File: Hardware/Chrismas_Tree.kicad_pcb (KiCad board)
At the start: 2 copper layers, 191 parts, among them U1 PIC18F23K22

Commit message: Added light bulbs schematic.
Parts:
- moved R75 7.62 mm to (176.5, 330.2), turned to 270 degrees
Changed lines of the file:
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@@
   )
   (module Resistor_THT:R_Axial_DIN0207_L6.3mm_D2.5mm_P7.62mm_Horizontal (layer B.Cu)
-    (at 176.53 337.82 90)
+    (at 176.53 330.2 270)
     (descr "Resistor, Axial_DIN0207 series, Axial, Horizontal, pin pitch=7.62mm, 0.25W = 1/4W, length*diameter=6.3*2.5mm^2, http://cdn-reichelt.de/documents/datenblatt/B400/1_4W%23YAG.pdf")
     (tags "Resistor Axial_DIN0207 series Axial Horizontal pin pitch 7.62mm 0.25W = 1/4W length 6.3mm diameter 2.5mm")
@@
     (fp_line (start 0.66 -1.25) (end 6.96 -1.25) (layer B.Fab) (width 0.1))
     (fp_line (start 0.66 1.25) (end 0.66 -1.25) (layer B.Fab) (width 0.1))
-    (pad 2 thru_hole oval (at 7.62 0 90) (size 1.6 1.6) (drill 0.8) (layers *.Cu *.Mask)
+    (pad 2 thru_hole oval (at 7.62 0 270) (size 1.6 1.6) (drill 0.8) (layers *.Cu *.Mask)
       (net 76 "Net-(D75-Pad2)"))
-    (pad 1 thru_hole circle (at 0 0 90) (size 1.6 1.6) (drill 0.8) (layers *.Cu *.Mask)
+    (pad 1 thru_hole circle (at 0 0 270) (size 1.6 1.6) (drill 0.8) (layers *.Cu *.Mask)
       (net 83 +5V))
     (model ${KISYS3DMOD}/Resistor_THT.3dshapes/R_Axial_DIN0207_L6.3mm_D2.5mm_P7.62mm_Horizontal.wrl

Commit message: Reorganized light bulbs connections to ease routing and placed microcontroller and related parts.
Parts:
- added C1: 100n-25V, Capacitor_THT:C_Disc_D5.0mm_W2.5mm_P5.00mm, B.Cu at (172.7, 210.8)
- added C2: 1u-25V, Capacitor_THT:C_Disc_D5.0mm_W2.5mm_P5.00mm, B.Cu at (172.7, 215.9)
- added C3: 10u-25V, Capacitor_THT:C_Disc_D5.0mm_W2.5mm_P5.00mm, B.Cu at (180.3, 213.4)
- added C4: 100n-25V, Capacitor_THT:C_Disc_D5.0mm_W2.5mm_P5.00mm, B.Cu at (157.5, 259.1)
- added J1: DNP, Connector_PinHeader_2.54mm:PinHeader_1x05_P2.54mm_Vertical, F.Cu at (167.6, 251.5)
- added Q1: BC548, Package_TO_SOT_THT:TO-92_Inline, B.Cu at (152.4, 17.8)
- added R96: 180, Resistor_THT:R_Axial_DIN0207_L6.3mm_D2.5mm_P7.62mm_Horizontal, B.Cu at (157.5, 182.9)
- added R97: 220, Resistor_THT:R_Axial_DIN0207_L6.3mm_D2.5mm_P7.62mm_Horizontal, B.Cu at (152.4, 241.3)
- added R98: 10K, Resistor_THT:R_Axial_DIN0207_L6.3mm_D2.5mm_P7.62mm_Horizontal, B.Cu at (160.0, 246.4)
- D92, D93, D94, D95: value LED -> RED
- R82, R83, R84, R85, R86, R87, R88, R89, R90, R91, R92, R93, R94, R95: value R -> 220; moved to B.Cu
- U1: moved to B.Cu
- moved R92 339.9 mm to (142.2, 10.2)
- moved R93 321.2 mm to (180.3, 10.2), turned to 180 degrees
- moved U1 309.2 mm to (157.5, 231.1)
- moved R94 297.7 mm to (175.3, 17.8), turned to 180 degrees
- moved R90 236.2 mm to (142.2, 215.9), turned to 180 degrees
- moved R95 224.9 mm to (175.3, 2.54), turned to 180 degrees
- moved R86 219.7 mm to (142.2, 205.7), turned to 180 degrees
- moved R88 219.4 mm to (142.2, 210.8), turned to 180 degrees
- moved R84 214.4 mm to (147.3, 203.2), turned to 90 degrees
- moved R83 209.1 mm to (165.1, 190.5), turned to 90 degrees
- moved R82 209.1 mm to (152.4, 200.7), turned to 90 degrees
- moved R85 202.4 mm to (170.2, 200.7), turned to 90 degrees
- moved R87 201.1 mm to (180.3, 203.2)
- moved R89 187.1 mm to (180.3, 226.1)
- moved R91 186.4 mm to (180.3, 233.7)
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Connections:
- D92 pad 1: GND -> Net-(D92-Pad1)
- D93 pad 1: GND -> Net-(D92-Pad1)
- D94 pad 1: GND -> Net-(D92-Pad1)
- D95 pad 1: GND -> Net-(D92-Pad1)
- R82 pad 1: Net-(R82-Pad1) -> /Light bulbs/Bulb_0
- R83 pad 1: Net-(R82-Pad1) -> /Light bulbs/Bulb_9
- R84 pad 1: Net-(R82-Pad1) -> /Light bulbs/Bulb_1
- R85 pad 1: Net-(R82-Pad1) -> /Light bulbs/Bulb_8
- R86 pad 1: Net-(R82-Pad1) -> /Light bulbs/Bulb_2
- R87 pad 1: Net-(R82-Pad1) -> /Light bulbs/Bulb_7
- R88 pad 1: Net-(R82-Pad1) -> /Light bulbs/Bulb_3
- R89 pad 1: Net-(R82-Pad1) -> /Light bulbs/Bulb_6
- R90 pad 1: Net-(R82-Pad1) -> /Light bulbs/Bulb_4
- R91 pad 1: Net-(R82-Pad1) -> /Light bulbs/Bulb_5
- R92 pad 1: Net-(R82-Pad1) -> +5V
- R93 pad 1: Net-(R82-Pad1) -> +5V
- R94 pad 1: Net-(R82-Pad1) -> +5V
- R95 pad 1: Net-(R82-Pad1) -> +5V
- U1 pad 10: Net-(U1-Pad10) -> /Light bulbs/Bulb_3
- U1 pad 11: Net-(U1-Pad11) -> /Light bulbs/Bulb_2
- U1 pad 12: Net-(U1-Pad12) -> /Light bulbs/Bulb_1
- U1 pad 13: Net-(U1-Pad13) -> /Light bulbs/Bulb_0
- U1 pad 14: Net-(U1-Pad14) -> /Light bulbs/Star
- U1 pad 15: Net-(U1-Pad15) -> /Light bulbs/Bulb_9
- U1 pad 16: Net-(U1-Pad16) -> /Light bulbs/Bulb_8
- U1 pad 17: Net-(U1-Pad17) -> /Light bulbs/Bulb_7
- U1 pad 19: Net-(U1-Pad19) -> GND
- U1 pad 20: Net-(U1-Pad20) -> +5V
- U1 pad 25: Net-(U1-Pad25) -> /Light bulbs/Bulb_6
- U1 pad 26: Net-(U1-Pad26) -> /Light bulbs/Bulb_5
- U1 pad 8: Net-(U1-Pad8) -> GND
- U1 pad 9: Net-(U1-Pad9) -> /Light bulbs/Bulb_4
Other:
- board text added: "/MCLR"

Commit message: Set foliage and trunk leds color.
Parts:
- D1, D10, D11, D12, D14, D15, D16, D18, D19, D2, D20, D22, D23, D24, D26, D27, D28, D3, D30, D31, D32, D34, D35, D36, D38, D39, D40, D42, D43, D44, D46, D47, D48, D50, D51, D52, D53, D54, D55, D56, D57, D58, D59, D6, D60, D61, D62, D63, D64, D65, D66, D67, D68, D69, D7, D70, D71, D72, D73, D74, D75, D76, D77, D78, D79, D8, D80, D81: value LED -> Green
- D13, D17, D21, D25, D29, D33, D37, D4, D41, D45, D49, D5, D9: value LED -> Amber
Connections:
- R13 pad 1: +5V -> Net-(R13-Pad1)
- R17 pad 1: +5V -> Net-(R13-Pad1)
- R21 pad 1: +5V -> Net-(R13-Pad1)
- R25 pad 1: +5V -> Net-(R13-Pad1)
- R29 pad 1: +5V -> Net-(R13-Pad1)
- R33 pad 1: +5V -> Net-(R13-Pad1)
- R37 pad 1: +5V -> Net-(R13-Pad1)
- R4 pad 1: +5V -> Net-(R13-Pad1)
- R41 pad 1: +5V -> Net-(R13-Pad1)
- R45 pad 1: +5V -> Net-(R13-Pad1)
- R49 pad 1: +5V -> Net-(R13-Pad1)
- R5 pad 1: +5V -> Net-(R13-Pad1)
- R9 pad 1: +5V -> Net-(R13-Pad1)

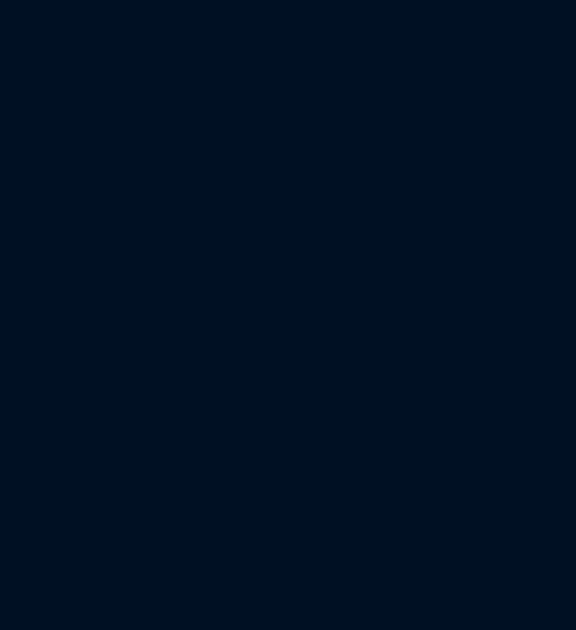
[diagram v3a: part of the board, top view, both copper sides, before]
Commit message: Added micro USB B connector for power supply.
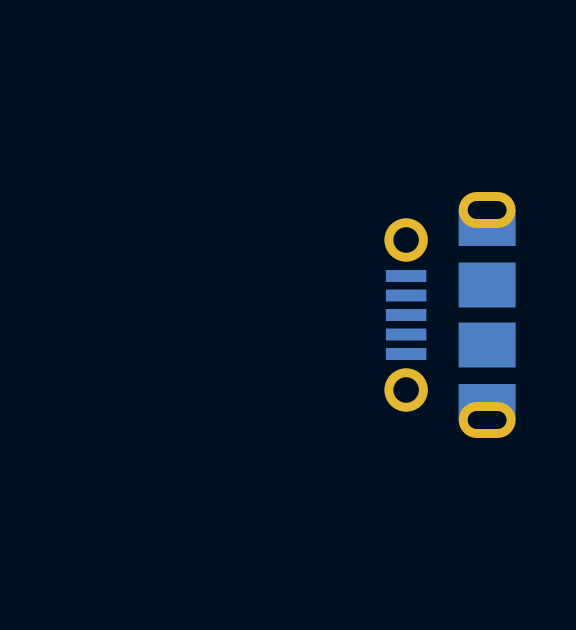
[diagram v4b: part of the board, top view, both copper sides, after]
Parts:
- added J2: USB_B_Micro, Connector_USB:USB_Micro-B_Molex-105017-0001, B.Cu at (289.6, 330.2)
- R1, R10, R11, R12, R13, R14, R15, R16, R17, R18, R19, R2, R20, R21, R22, R23, R24, R25, R26, R27, R28, R29, R3, R30, R31, R32, R33, R34, R35, R36, R37, R38, R39, R4, R40, R41, R42, R43, R44, R45, R46, R47, R48, R49, R5, R50, R51, R52, R53, R54, R55, R56, R57, R58, R59, R6, R60, R61, R62, R63, R64, R65, R66, R67, R68, R69, R7, R70, R71, R72, R73, R74, R75, R76, R77, R78, R79, R8, R80, R81, R9: value R -> 180

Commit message: Routed whole circuit and added ground planes.
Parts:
- moved J2 3.81 mm to (285.8, 330.2)
- renumbered D38 to D10, D42 to D11, D46 to D12, D50 to D13, D53 to D14, D56 to D15, D59 to D16, D62 to D17, D65 to D18, D68 to D19, D6 to D2, D71 to D20, D74 to D21, D76 to D22, D78 to D23, D80 to D24, D2 to D25, D7 to D26, D11 to D27, D15 to D28, D19 to D29, D10 to D3, D23 to D30, D27 to D31, D31 to D32, D35 to D33, D39 to D34, D43 to D35, D47 to D36, D51 to D37, D54 to D38, D57 to D39, D14 to D4, D60 to D40, D63 to D41, D66 to D42, D69 to D43, D72 to D44, D75 to D45, D77 to D46, D79 to D47, D81 to D48, D3 to D49, D18 to D5, D8 to D50, D12 to D51, D16 to D52, D20 to D53, D24 to D54, D28 to D55, D32 to D56, D36 to D57, D40 to D58, D44 to D59, D22 to D6, D48 to D60, D52 to D61, D55 to D62, D58 to D63, D61 to D64, D64 to D65, D67 to D66, D70 to D67, D73 to D68, D4 to D69, D26 to D7, D5 to D70, D9 to D71, D13 to D72, D17 to D73, D21 to D74, D25 to D75, D29 to D76, D33 to D77, D37 to D78, D41 to D79, D30 to D8, D45 to D80, D49 to D81, D34 to D9, R38 to R10, R42 to R11, R46 to R12, R50 to R13, R53 to R14, R56 to R15, R59 to R16, R62 to R17, R65 to R18, R68 to R19, R6 to R2, R71 to R20, R74 to R21, R76 to R22, R78 to R23, R80 to R24, R2 to R25, R7 to R26, R11 to R27, R15 to R28, R19 to R29, R10 to R3, R23 to R30, R27 to R31, R31 to R32, R35 to R33, R39 to R34, R43 to R35, R47 to R36, R51 to R37, R54 to R38, R57 to R39, R14 to R4, R60 to R40, R63 to R41, R66 to R42, R69 to R43, R72 to R44, R75 to R45, R77 to R46, R79 to R47, R81 to R48, R3 to R49, R18 to R5, R8 to R50, R12 to R51, R16 to R52, R20 to R53, R24 to R54, R28 to R55, R32 to R56, R36 to R57, R40 to R58, R44 to R59, R22 to R6, R48 to R60, R52 to R61, R55 to R62, R58 to R63, R61 to R64, R64 to R65, R67 to R66, R70 to R67, R73 to R68, R4 to R69, R26 to R7, R5 to R70, R9 to R71, R13 to R72, R17 to R73, R21 to R74, R25 to R75, R29 to R76, R33 to R77, R37 to R78, R41 to R79, R30 to R8, R45 to R80, R49 to R81, R34 to R9
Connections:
- R69 pad 1: Net-(R13-Pad1) -> +5V
- R70 pad 1: Net-(R13-Pad1) -> +5V
- R71 pad 1: Net-(R13-Pad1) -> +5V
- R72 pad 1: Net-(R13-Pad1) -> +5V
- R73 pad 1: Net-(R13-Pad1) -> +5V
- R74 pad 1: Net-(R13-Pad1) -> +5V
- R75 pad 1: Net-(R13-Pad1) -> +5V
- R76 pad 1: Net-(R13-Pad1) -> +5V
- R77 pad 1: Net-(R13-Pad1) -> +5V
- R78 pad 1: Net-(R13-Pad1) -> +5V
- R79 pad 1: Net-(R13-Pad1) -> +5V
- R80 pad 1: Net-(R13-Pad1) -> +5V
- R81 pad 1: Net-(R13-Pad1) -> +5V
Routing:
- net +5V: track 0.00 -> 1501.5 mm
- net Net-(Q1-Pad2): track 0.00 -> 167.0 mm
- net Net-(D82-Pad2): track 0.00 -> 131.1 mm
- net Net-(D88-Pad2): track 0.00 -> 122.1 mm
- net Net-(D83-Pad2): track 0.00 -> 114.3 mm
- net Net-(D89-Pad2): track 0.00 -> 103.7 mm
- net Net-(D90-Pad2): track 0.00 -> 100.4 mm
- net Net-(D85-Pad2): track 0.00 -> 89.0 mm
- net Net-(D91-Pad2): track 0.00 -> 77.3 mm
- net Net-(D87-Pad2): track 0.00 -> 72.2 mm
- net Net-(D84-Pad2): track 0.00 -> 70.2 mm
- net Net-(D86-Pad2): track 0.00 -> 59.4 mm
- net Net-(D92-Pad1): track 0.00 -> 32.6 mm
- net Net-(J1-Pad1): track 0.00 -> 32.6 mm
- net Net-(J1-Pad2): track 0.00 -> 20.3 mm
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- added copper zone on B.Cu, net GND
- added copper zone on F.Cu, net GND
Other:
- board text added: "11/2019"

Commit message: Fixed PCB title block.
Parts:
- moved D83 33.3 mm to (204.7, 128.3)
- moved C1 33.3 mm to (173.5, 244.1)
- moved C2 33.3 mm to (173.5, 249.2)
- moved C4 33.3 mm to (158.2, 292.4)
- moved D1 33.3 mm to (162.1, 59.9)
- moved D10 33.3 mm to (73.2, 221.2)
- moved D12 33.3 mm to (106.7, 264.4)
- moved D15 33.3 mm to (53.8, 306.1)
- moved D16 33.3 mm to (247.7, 312.7)
- moved D17 33.3 mm to (111.3, 320.3)
- moved D18 33.3 mm to (193.8, 323.1)
- moved D19 33.3 mm to (160.8, 318.3)
- moved D2 33.3 mm to (135.4, 93.0)
- moved D20 33.3 mm to (186.4, 347.0)
- moved D21 33.3 mm to (137.4, 358.4)
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
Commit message: Added PCB edges cut.
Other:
- board outline added: 261.6 x 368.3 mm
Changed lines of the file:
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@@
   (general
     (thickness 1.6)
-    (drawings 2)
+    (drawings 7)
     (tracks 403)
     (zones 0)
@@
     )
   )
+  (gr_line (start 28.956 393.954) (end 290.322 393.954) (layer Edge.Cuts) (width 0.05))
+  (gr_line (start 28.702 393.954) (end 28.956 393.954) (layer Edge.Cuts) (width 0.05))
+  (gr_line (start 28.702 25.654) (end 28.702 393.954) (layer Edge.Cuts) (width 0.05))
+  (gr_line (start 290.322 25.654) (end 28.702 25.654) (layer Edge.Cuts) (width 0.05))
+  (gr_line (start 290.322 393.954) (end 290.322 25.654) (layer Edge.Cuts) (width 0.05))
   (gr_text 11/2019 (at 282.702 388.874) (layer F.SilkS)
     (effects (font (size 1 1) (thickness 0.15)))

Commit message: Resized board to center the tree in the PCB middle.
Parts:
- moved J2 3.05 mm to (289.6, 363.5)
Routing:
- net GND: track 10.1 -> 11.9 mm
- net +5V: track 1501.5 -> 1502.3 mm
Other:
- board size 261.6 x 368.3 mm -> 264.4 x 368.3 mm
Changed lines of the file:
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@@
     (thickness 1.6)
     (drawings 7)
-    (tracks 403)
+    (tracks 404)
     (zones 0)
     (modules 201)
@@
   )
   (setup
-    (last_trace_width 0.25)
+    (last_trace_width 0.4)
     (user_trace_width 0.4)
     (user_trace_width 1)
@@
   )
   (module Connector_USB:USB_Micro-B_Molex-105017-0001 (layer B.Cu)
-    (at 286.512 363.474 270)
+    (at 289.56 363.474 270)
     (descr http://www.molex.com/pdm_docs/sd/1050170001_sd.pdf)
     (tags "Micro-USB SMD Typ-B")
@@
     )
   )
-  (gr_line (start 28.956 393.954) (end 290.322 393.954) (layer Edge.Cuts) (width 0.05))
+  (gr_line (start 28.956 393.954) (end 293.116 393.954) (layer Edge.Cuts) (width 0.05))
   (gr_line (start 28.702 393.954) (end 28.956 393.954) (layer Edge.Cuts) (width 0.05))
   (gr_line (start 28.702 25.654) (end 28.702 393.954) (layer Edge.Cuts) (width 0.05))
-  (gr_line (start 290.322 25.654) (end 28.702 25.654) (layer Edge.Cuts) (width 0.05))
-  (gr_line (start 290.322 393.954) (end 290.322 25.654) (layer Edge.Cuts) (width 0.05))
+  (gr_line (start 293.116 25.654) (end 28.702 25.654) (layer Edge.Cuts) (width 0.05))
+  (gr_line (start 293.116 393.954) (end 293.116 25.654) (layer Edge.Cuts) (width 0.05))
   (gr_text 11/2019 (at 282.702 388.874) (layer F.SilkS)
     (effects (font (size 1 1) (thickness 0.15)))
@@
   (segment (start 163.322 284.734) (end 163.322 292.354) (width 1.5) (layer B.Cu) (net 25))
   (segment (start 163.322 292.354) (end 163.242 292.354) (width 1.5) (layer B.Cu) (net 25))
-  (segment (start 283.9745 364.774) (end 283.9445 364.744) (width 0.4) (layer B.Cu) (net 25))
-  (segment (start 285.0495 364.774) (end 283.9745 364.774) (width 0.4) (layer B.Cu) (net 25))
-  (segment (start 283.9445 364.744) (end 282.702 364.744) (width 0.4) (layer B.Cu) (net 25))
+  (segment (start 287.0225 364.774) (end 286.7985 364.998) (width 0.4) (layer B.Cu) (net 25))
+  (segment (start 288.0975 364.774) (end 287.0225 364.774) (width 0.4) (layer B.Cu) (net 25))
+  (segment (start 290.4975 364.774) (end 290.7975 364.474) (width 0.4) (layer B.Cu) (net 25))
+  (segment (start 288.0975 364.774) (end 290.4975 364.774) (width 0.4) (layer B.Cu) (net 25))
   (segment (start 154.432 71.374) (end 154.432 78.232) (width 1.5) (layer B.Cu) (net 26))
   (segment (start 181.61 92.964) (end 186.182 92.964) (width 1.5) (layer B.Cu) (net 27))
@@
   (segment (start 281.432 308.864) (end 281.432 359.664) (width 1.5) (layer B.Cu) (net 83))
   (segment (start 281.432 359.664) (end 281.432 360.934) (width 1.5) (layer B.Cu) (net 83))
-  (segment (start 285.0495 362.174) (end 282.732 362.174) (width 0.25) (layer B.Cu) (net 83))
   (segment (start 281.492 360.934) (end 281.432 360.934) (width 0.25) (layer B.Cu) (net 83))
   (segment (start 281.492 360.934) (end 281.492 360.994) (width 1.5) (layer B.Cu) (net 83))
-  (segment (start 281.492 360.994) (end 282.672 362.174) (width 1.5) (layer B.Cu) (net 83))
+  (segment (start 281.522 361.024) (end 282.702 362.204) (width 1.5) (layer B.Cu) (net 83))
   (segment (start 282.672 362.174) (end 282.732 362.174) (width 0.4) (layer B.Cu) (net 83))
-  (segment (start 282.672 362.174) (end 285.0495 362.174) (width 0.4) (layer B.Cu) (net 83))
+  (segment (start 286.4205 362.174) (end 288.798 362.174) (width 0.4) (layer B.Cu) (net 83))
+  (segment (start 282.672 362.174) (end 285.72 362.174) (width 1.5) (layer B.Cu) (net 83))
   (segment (start 153.162 155.194) (end 153.162 226.314) (width 1.5) (layer F.Cu) (net 84))
   (segment (start 120.142 150.114) (end 148.082 150.114) (width 1.5) (layer F.Cu) (net 84))
@@
     (polygon
       (pts
-        (xy 28.702 25.654) (xy 290.322 25.654) (xy 290.322 393.954) (xy 28.702 393.954)
+        (xy 28.702 25.654) (xy 293.116 25.654) (xy 293.116 393.954) (xy 28.702 393.954)
       )
     )
@@
     (polygon
       (pts
-        (xy 28.702 25.654) (xy 290.322 25.654) (xy 290.322 393.954) (xy 28.702 393.954)
+        (xy 28.702 25.654) (xy 293.116 25.654) (xy 293.116 393.954) (xy 28.702 393.954)
       )
     )
